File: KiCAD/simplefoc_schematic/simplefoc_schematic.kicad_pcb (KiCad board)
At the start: 2 copper layers, 51.9 x 74.3 mm, 49 parts, among them J1 Power Supply, J2 Motor Connector, J3 Sensor Connector, J5 Programming Port, J6 UART Port, J7 Conn_01x03, Q1 IRF740, Q2 IRF740, Q3 IRF740, Q4 IRF740, Q5 IRF740, Q6 IRF740, U1 IR2130, U2 STM32F101CBT6, U3 LM317L_SOT-89, U4 TS 1117

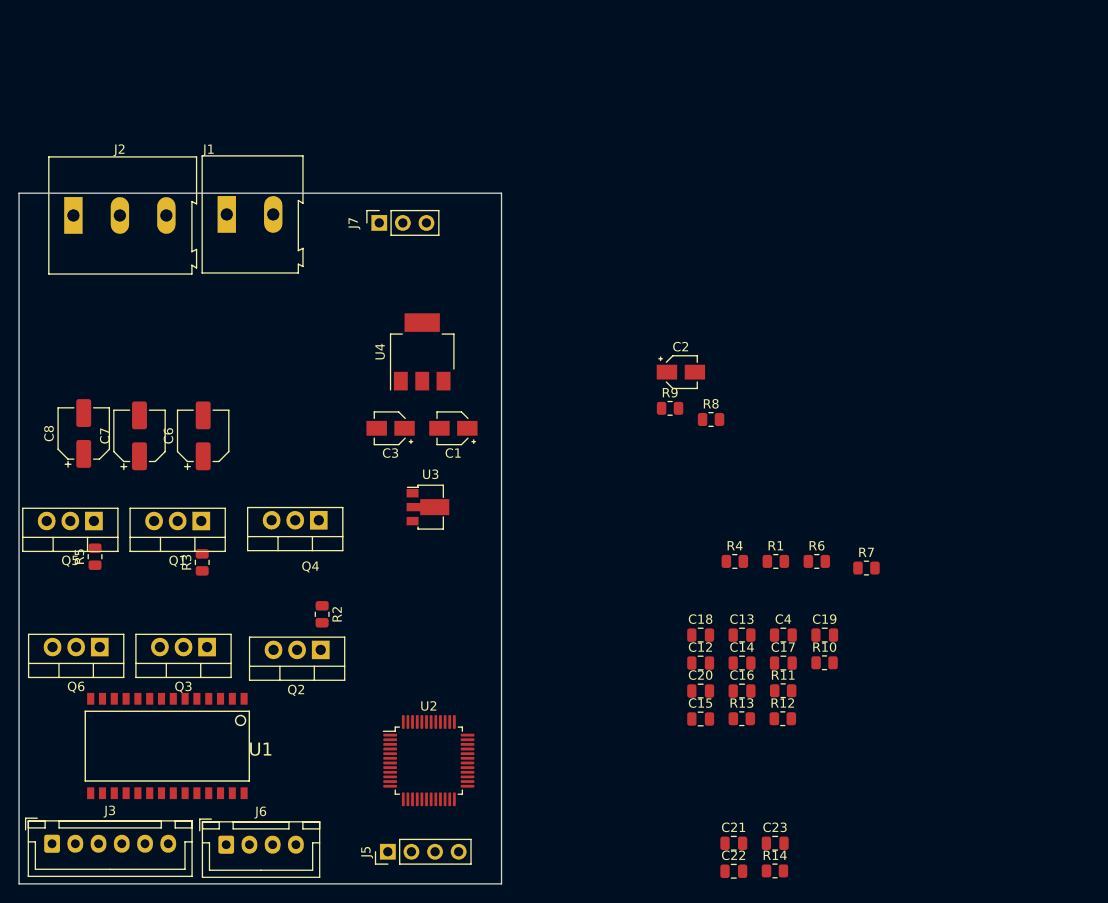
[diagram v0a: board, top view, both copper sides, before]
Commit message: Added a standalone schematic for the STM32 part Moved from ir2130 driver to the TMC6140
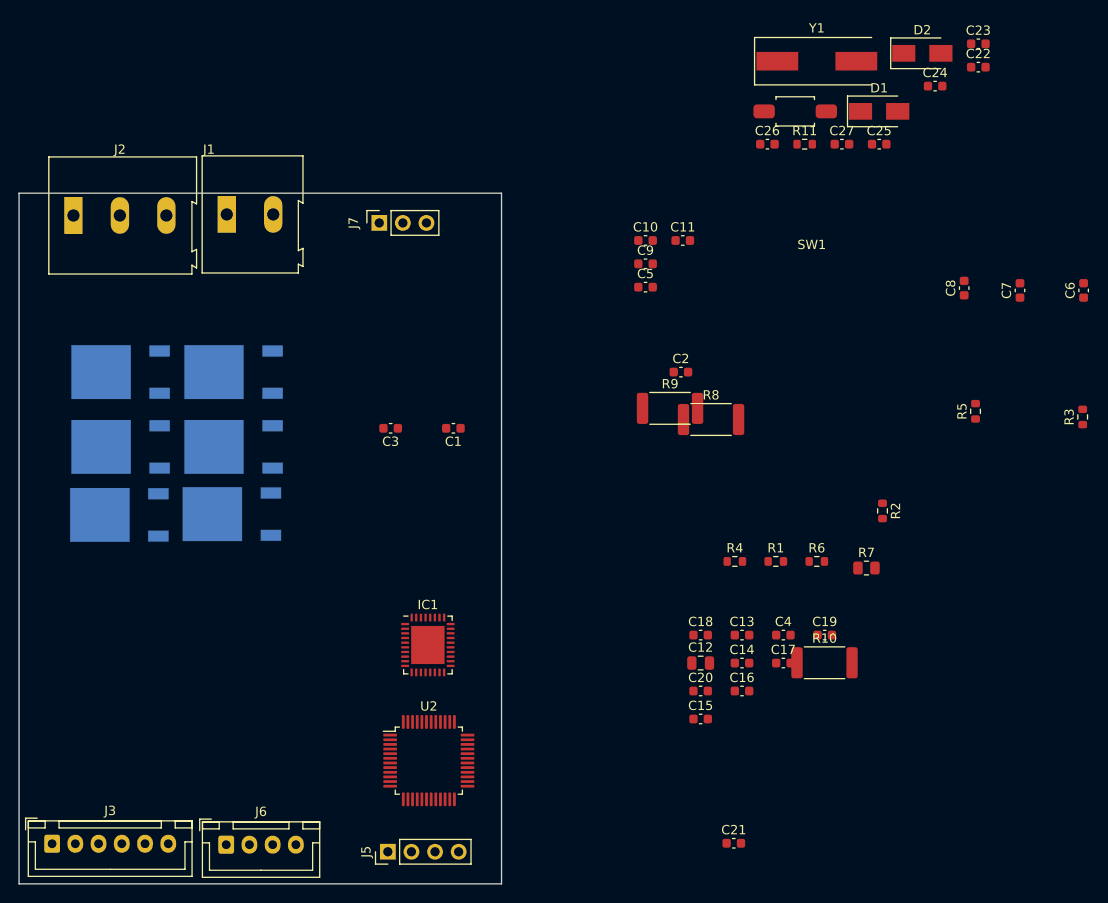
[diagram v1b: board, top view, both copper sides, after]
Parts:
- removed R12: 1k, Resistor_SMD:R_0805_2012Metric
- removed R13, R14: ?, Resistor_SMD:R_0805_2012Metric
- removed U1: IR2130, Additional_Components:SO-28W
- removed U3: LM317L_SOT-89, Package_TO_SOT_SMD:SOT-89-3
- removed U4: TS 1117, Package_TO_SOT_SMD:SOT-223
- added C10: 1nF/50V, Capacitor_SMD:C_0603_1608Metric, F.Cu at (239.4, 50.9)
- added C11: 1nF/50V, Capacitor_SMD:C_0603_1608Metric, F.Cu at (243.4, 50.9)
- added C24: 100nF/35V, Capacitor_SMD:C_0603_1608Metric, F.Cu at (270.6, 34.2)
- added C25: 20uF/6.3V, Capacitor_SMD:C_0603_1608Metric, F.Cu at (264.6, 40.5)
- added C26: 20uF/6.3V, Capacitor_SMD:C_0603_1608Metric, F.Cu at (252.5, 40.5)
- added C27: 100nF/35V, Capacitor_SMD:C_0603_1608Metric, F.Cu at (260.6, 40.5)
- added C5: 1uF, Capacitor_SMD:C_0603_1608Metric, F.Cu at (239.4, 55.9)
- added C9: 470nF/16V, Capacitor_SMD:C_0603_1608Metric, F.Cu at (239.4, 53.4)
- added D1: D_Schottky, Diode_SMD:D_SMA, F.Cu at (264.6, 37.0)
- added D2: D_Schottky, Diode_SMD:D_SMA, F.Cu at (269.2, 30.7)
- added IC1: TMC6140-Trinamic, Package_DFN_QFN:QFN-36-1EP_5x6mm_P0.5mm_EP3.6x4.1mm, F.Cu at (216.0, 94.4)
- added SW1: SW_Push, Additional_Components:SW_Push_SPST_Wuerth_434121043816, F.Cu at (255.5, 37.0)
- added Y1: 8MHz, Crystal:Crystal_SMD_HC49-SD, F.Cu at (257.9, 31.6)
- C1: value 47uF -> 100nF; footprint Capacitor_SMD:CP_Elec_3x5.3 -> Capacitor_SMD:C_0603_1608Metric
- C13, C18, C4: footprint Capacitor_SMD:C_0805_2012Metric -> Capacitor_SMD:C_0603_1608Metric
- C14: value 2.2uF -> 10uF; footprint Capacitor_SMD:C_0805_2012Metric -> Capacitor_SMD:C_0603_1608Metric
- C15, C17, C22, C23: value 2.2uF -> 100nF/35V; footprint Capacitor_SMD:C_0805_2012Metric -> Capacitor_SMD:C_0603_1608Metric
- C16, C21: value 2.2uF -> 10uF/35V; footprint Capacitor_SMD:C_0805_2012Metric -> Capacitor_SMD:C_0603_1608Metric
- C19: value 100nF -> 10uF/35V; footprint Capacitor_SMD:C_0805_2012Metric -> Capacitor_SMD:C_0603_1608Metric
- C2: value 10uF -> 100nF; footprint Capacitor_SMD:CP_Elec_3x5.3 -> Capacitor_SMD:C_0603_1608Metric
- C20: value 4.7uF -> 100nF/35V; footprint Capacitor_SMD:C_0805_2012Metric -> Capacitor_SMD:C_0603_1608Metric
- C3: value 10uF -> 10nF; footprint Capacitor_SMD:CP_Elec_3x5.3 -> Capacitor_SMD:C_0603_1608Metric
- C6, C7: value 220uF/63V -> 470nF/16V; footprint Capacitor_SMD:CP_Elec_5x3 -> Capacitor_SMD:C_0603_1608Metric
- C8: value 220uF/63V -> 1nF/50V; footprint Capacitor_SMD:CP_Elec_5x3 -> Capacitor_SMD:C_0603_1608Metric
- Q1, Q2, Q3, Q4, Q5, Q6: value IRF740 -> IRLR 2905; footprint Package_TO_SOT_THT:TO-220-3_Vertical -> Package_TO_SOT_SMD:TO-252-2; moved to B.Cu
- R1, R3, R4, R5, R6: value 4.7R -> 2.2R; footprint Resistor_SMD:R_0805_2012Metric -> Resistor_SMD:R_0603_1608Metric
- R10, R9: value 10k -> 1mOhm/3W; footprint Resistor_SMD:R_0805_2012Metric -> Resistor_SMD:R_2512_6332Metric
- R11: value 100k -> 2.2R; footprint Resistor_SMD:R_0805_2012Metric -> Resistor_SMD:R_0603_1608Metric
- R2: value 4.7R -> 4.7k; footprint Resistor_SMD:R_0805_2012Metric -> Resistor_SMD:R_0603_1608Metric
- R7: value 0.05R/5W -> FBead
- R8: value 1k -> 1mOhm/3W; footprint Resistor_SMD:R_0805_2012Metric -> Resistor_SMD:R_2512_6332Metric
- moved C7 96.0 mm to (279.7, 56.2)
- moved R3 96.0 mm to (286.5, 69.8)
- moved C6 96.0 mm to (286.6, 56.2)
- moved C8 96.0 mm to (273.7, 56.0)
- moved R5 96.0 mm to (274.9, 69.2)
- moved C22 90.4 mm to (275.2, 32.2)
- moved C23 88.8 mm to (275.2, 29.7)
- moved R2 61.3 mm to (264.9, 80.0)
- moved R11 58.9 mm to (256.5, 40.5)
- moved Q2 23.8 mm to (195.1, 73.1)
- moved Q6 20.2 mm to (194.9, 80.3)
- moved Q4 18.4 mm to (195.1, 65.0)
- moved Q3 17.1 mm to (182.8, 80.4)
- moved Q5 16.3 mm to (182.9, 65.0)
- moved Q1 11.8 mm to (182.9, 73.1)
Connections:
- net OSCIN renamed Net-(C13-Pad2)
- net OSCOUT renamed Net-(C18-Pad2)
- C14 pad 1: +3.3V -> Net-(C14-Pad1)
- C15 pad 1: +3.3V -> GND
- C15 pad 2: GND -> +BATT
- C16 pad 1: +3.3V -> GND
- C16 pad 2: GND -> +BATT
- C17 pad 1: +3.3V -> GND
- C17 pad 2: GND -> +BATT
- C19 pad 1: +3.3V -> GND
- C19 pad 2: GND -> +BATT
- C2 pad 1: +BATT -> +3.3V
- C2 pad 2: Net-(C2-Pad2) -> GND
- C20 pad 1: +BATT -> GND
- C20 pad 2: GND -> +BATT
- C21 pad 1: +3.3V -> GND
- C21 pad 2: GND -> +BATT
- C22 pad 1: +3.3V -> Net-(C22-Pad1)
- C22 pad 2: GND -> Net-(IC1-Pad10)
- C23 pad 1: +3.3V -> GND
- C23 pad 2: GND -> +BATT
- C3 pad 1: +BATT -> Net-(C3-Pad1)
- C4 pad 1: RESET -> Net-(C4-Pad1)
- C6 pad 1: +BATT -> Net-(C6-Pad1)
- C6 pad 2: GND -> U
- C7 pad 1: +BATT -> Net-(C7-Pad1)
- C7 pad 2: GND -> V
- C8 pad 1: +BATT -> U
- J3 pad 2: SC -> ENCC
- J3 pad 3: SB -> ENCB
- J3 pad 4: SA -> ENCA
- Q1 pad 3: W -> V
- Q2 pad 3: V -> W
- Q4 pad 2: W -> U
- Q4 pad 3: VS0 -> SensU
- Q5 pad 3: VS0 -> SensV
- Q6 pad 2: U -> W
- Q6 pad 3: VS0 -> SensW
- R1 pad 1: HOUT1 -> HOUTU
- R10 pad 1: +3.3V -> SensW
- R10 pad 2: RESET -> GND
- R11 pad 1: BOOT0 -> LOUTW
- R11 pad 2: Net-(J4-Pad3) -> Net-(Q6-Pad1)
- R2 pad 1: HOUT2 -> ENABLE
- R2 pad 2: Net-(Q2-Pad1) -> GND
- R3 pad 1: HOUT3 -> HOUTV
- R4 pad 1: LOUT1 -> HOUTW
- R4 pad 2: Net-(Q6-Pad1) -> Net-(Q2-Pad1)
- R5 pad 1: LOUT2 -> LOUTU
- R5 pad 2: Net-(Q5-Pad1) -> Net-(Q4-Pad1)
- R6 pad 1: LOUT3 -> LOUTV
- R6 pad 2: Net-(Q4-Pad1) -> Net-(Q5-Pad1)
- R7 pad 1: GND -> +3.3V
- R7 pad 2: VS0 -> Net-(C3-Pad1)
- R8 pad 1: +15V -> SensV
- R8 pad 2: Net-(R8-Pad2) -> GND
- R9 pad 1: Net-(R8-Pad2) -> SensU
- U2 pad 11: unconnected-(U2-Pad11) -> HO1
- U2 pad 12: unconnected-(U2-Pad12) -> LO1
- U2 pad 13: unconnected-(U2-Pad13) -> HO2
- U2 pad 14: unconnected-(U2-Pad14) -> LO2
- U2 pad 15: unconnected-(U2-Pad15) -> HO3
- U2 pad 16: unconnected-(U2-Pad16) -> LO3
- U2 pad 25: unconnected-(U2-Pad25) -> ENCA
- U2 pad 26: unconnected-(U2-Pad26) -> ENCB
- U2 pad 27: unconnected-(U2-Pad27) -> ENCC
- U2 pad 44: BOOT0 -> GND
- U2 pad 7: RESET -> Net-(C4-Pad1)
- U2 pad 9: +3.3V -> Net-(C3-Pad1)

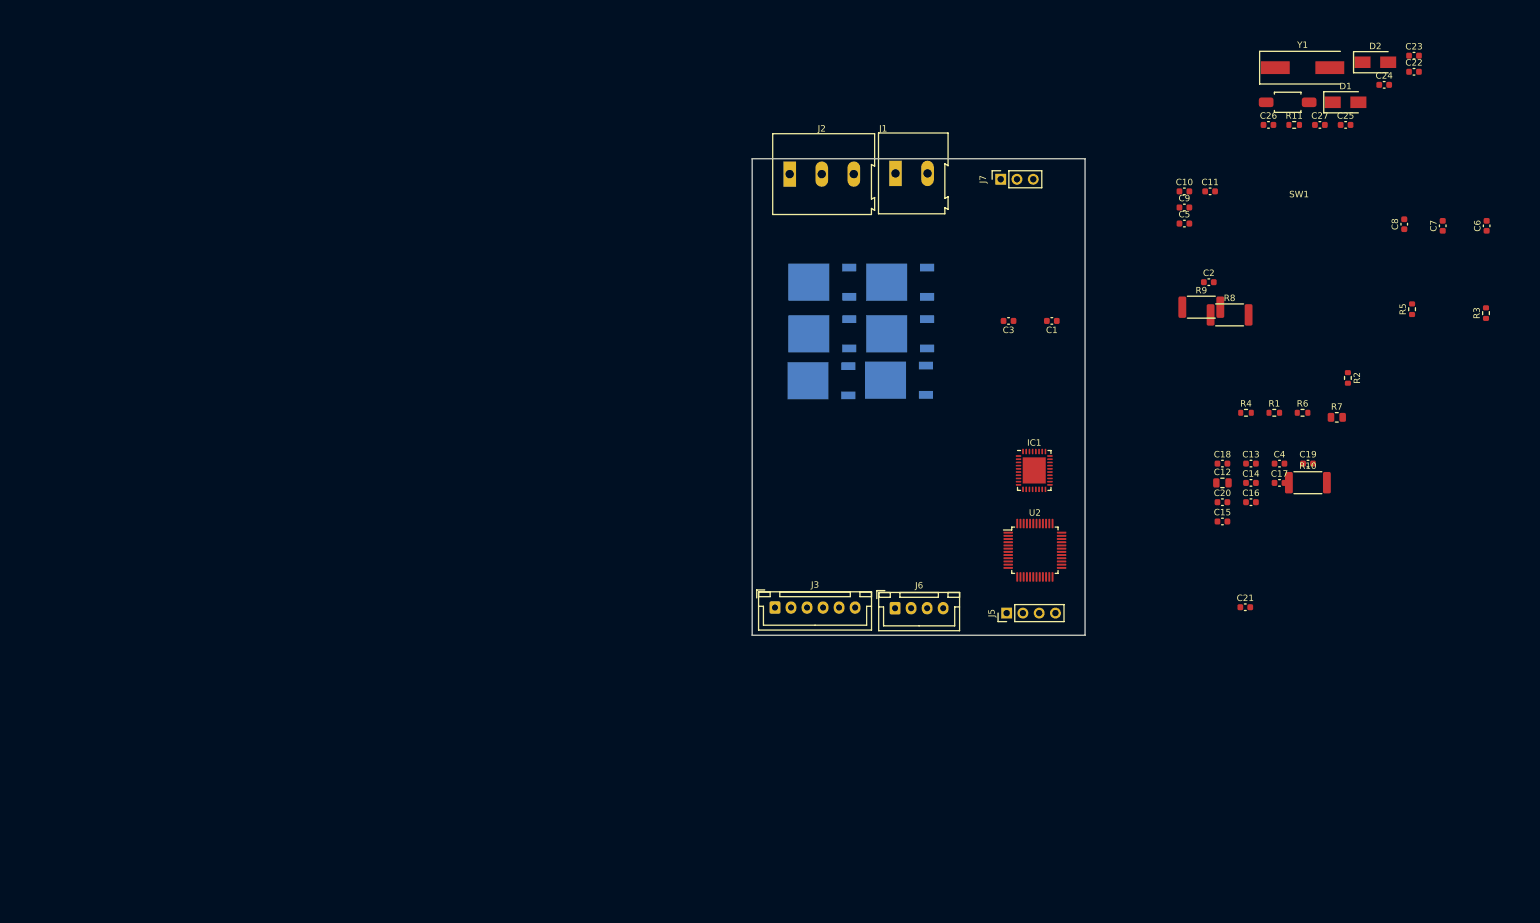
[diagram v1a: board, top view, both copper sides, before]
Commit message: Finalized schematic and component selection for acquisition from distributor
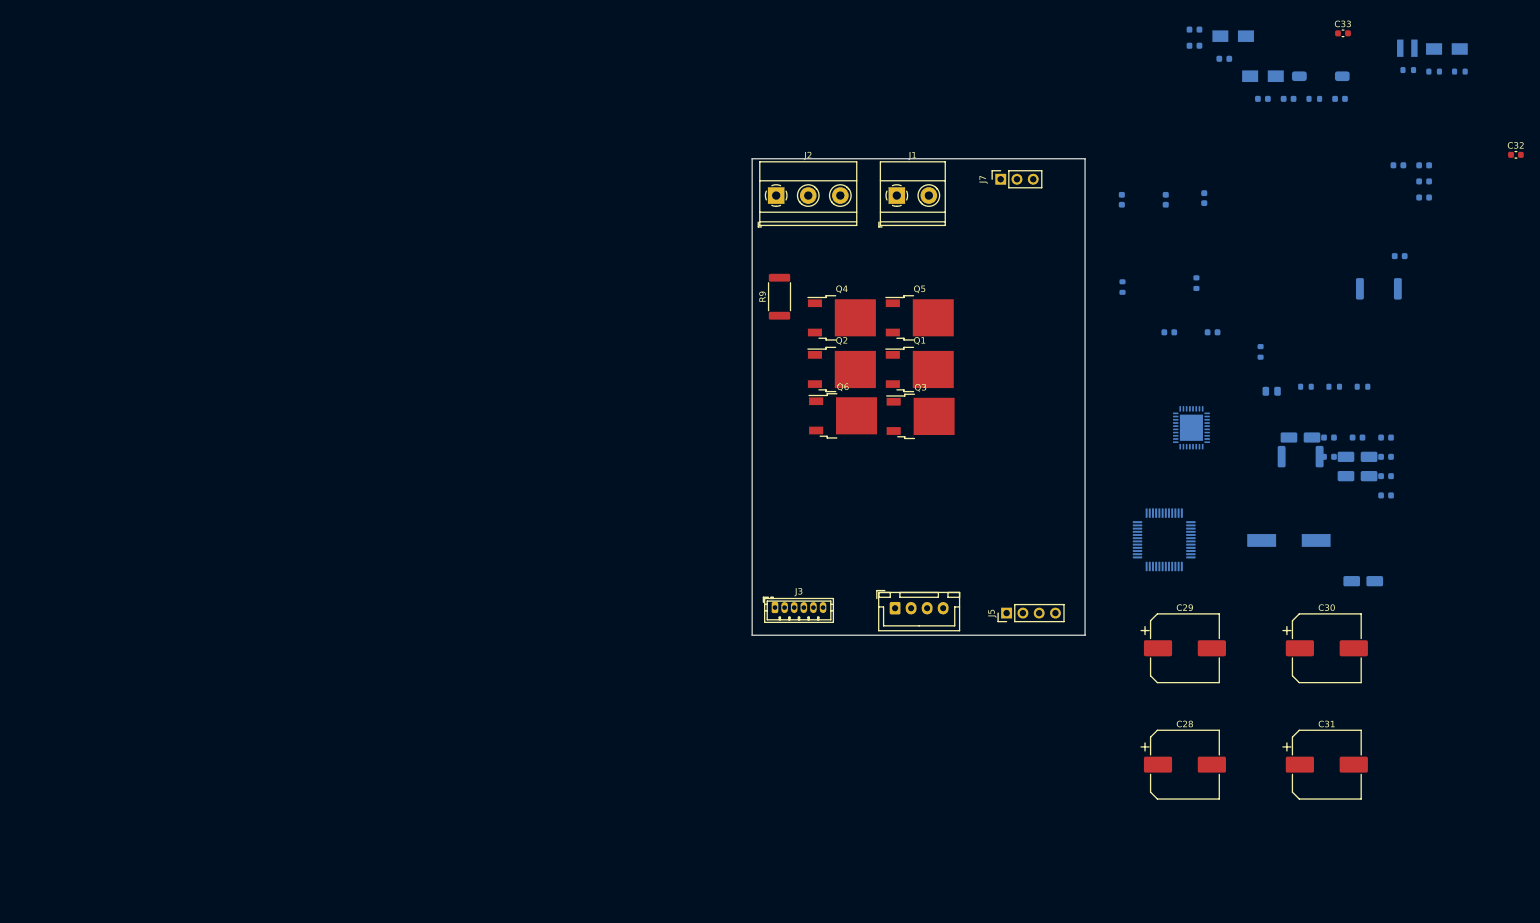
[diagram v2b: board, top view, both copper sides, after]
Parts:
- added C28: 1000uF/25V, Capacitor_SMD:CP_Elec_10x14.3, F.Cu at (239.5, 140.3)
- added C29: 1000uF/25V, Capacitor_SMD:CP_Elec_10x14.3, F.Cu at (239.5, 122.1)
- added C30: 1000uF/25V, Capacitor_SMD:CP_Elec_10x14.3, F.Cu at (261.6, 122.1)
- added C31: 1000uF/25V, Capacitor_SMD:CP_Elec_10x14.3, F.Cu at (261.6, 140.3)
- added C32: 100nF/35V, Capacitor_SMD:C_0603_1608Metric, F.Cu at (291.1, 45.2)
- added C33: 10uF/6.3V, Capacitor_SMD:C_0603_1608Metric, F.Cu at (264.2, 26.2)
- added D3: D_Schottky, Diode_SMD:D_SMA, B.Cu at (280.4, 28.7)
- added L1: 33uH/0.42A, Additional_Components:L_Fastron_1212_FPS, B.Cu at (274.2, 28.5)
- added R12: 47k, Resistor_SMD:R_0603_1608Metric, B.Cu at (274.3, 31.9)
- added R13: 47k, Resistor_SMD:R_0603_1608Metric, B.Cu at (278.4, 32.2)
- added R14: 47k, Resistor_SMD:R_0603_1608Metric, B.Cu at (282.4, 32.2)
- C1, C2, C4: value 100nF -> 100nF/6V; moved to B.Cu
- C10, C11, C15, C17, C20, C22, C23, C24, C27, C6, C7, C8, C9, D1, D2, IC1, R1, R10, R11, R2, R3, R4, R5, R6, R7, R8, SW1, U2, Y1: moved to B.Cu
- C12: value 100nF -> 100nF/35V; footprint Capacitor_SMD:C_0805_2012Metric -> Capacitor_SMD:C_0603_1608Metric; moved to B.Cu
- C13, C18: value 20pF -> 20pF/6V; moved to B.Cu
- C14: value 10uF -> 10uF/35V; footprint Capacitor_SMD:C_0603_1608Metric -> Capacitor_SMD:CP_Elec_4x5.8; moved to B.Cu
- C16, C19, C21: footprint Capacitor_SMD:C_0603_1608Metric -> Capacitor_SMD:CP_Elec_4x5.8; moved to B.Cu
- C25, C26: value 20uF/6.3V -> 10uF/6.3V; moved to B.Cu
- C3: value 10nF -> 10nF/6V; moved to B.Cu
- C5: value 1uF -> 1uF/6V; moved to B.Cu
- J1: footprint TerminalBlock:TerminalBlock_Altech_AK300-2_P5.00mm -> TerminalBlock_Phoenix:TerminalBlock_Phoenix_MKDS-1,5-2_1x02_P5.00mm_Horizontal
- J2: footprint TerminalBlock:TerminalBlock_Altech_AK300-3_P5.00mm -> TerminalBlock_Phoenix:TerminalBlock_Phoenix_MKDS-1,5-3_1x03_P5.00mm_Horizontal
- J3: footprint Connector_JST:JST_XH_B6B-XH-A_1x06_P2.50mm_Vertical -> Connector_JST:JST_ZH_B6B-ZR_1x06_P1.50mm_Vertical
- Q1, Q2, Q3, Q4, Q5, Q6: moved to F.Cu
- moved Y1 73.8 mm to (255.7, 105.3), turned to 180 degrees
- moved R9 65.8 mm to (176.3, 67.3), turned to 90 degrees
- moved C6 57.0 mm to (229.7, 52.2)
- moved R3 56.8 mm to (229.8, 65.8)
- moved C7 43.4 mm to (236.5, 52.2)
- moved C10 37.6 mm to (276.8, 46.8), turned to 180 degrees
- moved C5 37.6 mm to (276.8, 51.8), turned to 180 degrees
- moved C9 37.6 mm to (276.8, 49.3), turned to 180 degrees
- moved C22 34.5 mm to (241.0, 28.1), turned to 180 degrees
- moved C23 34.5 mm to (241.0, 25.6), turned to 180 degrees
- moved R5 33.9 mm to (241.3, 65.2)
- moved C3 31.9 mm to (243.8, 72.8), turned to 0 degrees
- moved C8 31.5 mm to (242.5, 51.9)
- moved C2 30.0 mm to (273.0, 61.0), turned to 180 degrees
- moved C11 29.6 mm to (272.8, 46.8), turned to 180 degrees
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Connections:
- IC1 pad 19: unconnected-(IC1-Pad19) -> Net-(IC1-Pad19)
- U2 pad 17: unconnected-(U2-Pad17) -> CURRW
- U2 pad 18: unconnected-(U2-Pad18) -> CURRU
- U2 pad 19: unconnected-(U2-Pad19) -> CURRV
